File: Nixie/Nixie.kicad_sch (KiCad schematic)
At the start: 43 parts

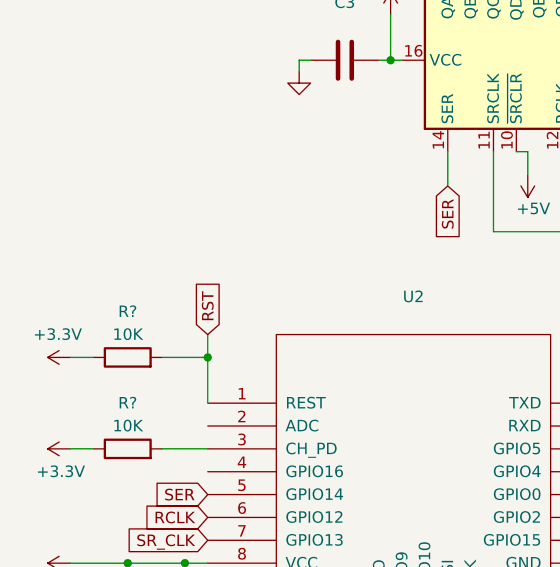
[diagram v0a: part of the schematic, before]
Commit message: Reset Knopf hinzugefügt
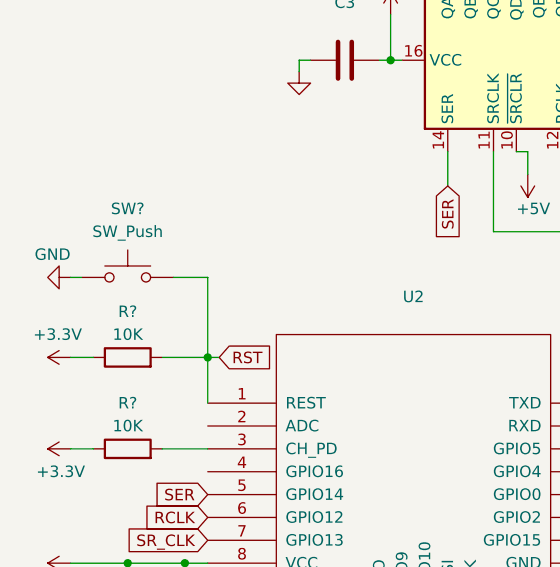
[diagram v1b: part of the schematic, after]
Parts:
- added SW?: SW_Push, symbol Switch:SW_Push
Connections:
- net GND: now also SW?.1
- net RST: now also SW?.2
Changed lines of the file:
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@@
     (stroke (width 0) (type default) (color 0 0 0 0))
   )
-  (wire (pts (xy 33.02 130.81) (xy 33.02 133.35))
+  (wire (pts (xy 34.29 133.35) (xy 33.02 133.35))
     (stroke (width 0) (type default) (color 0 0 0 0))
   )
@@
     (stroke (width 0) (type default) (color 0 0 0 0))
   )
+  (wire (pts (xy 33.02 124.46) (xy 29.21 124.46))
+    (stroke (width 0) (type default) (color 0 0 0 0))
+  )
   (wire (pts (xy 101.6 121.92) (xy 163.83 121.92))
     (stroke (width 0) (type default) (color 0 0 0 0))
@@
     (stroke (width 0) (type default) (color 0 0 0 0))
   )
+  (wire (pts (xy 33.02 133.35) (xy 33.02 124.46))
+    (stroke (width 0) (type default) (color 0 0 0 0))
+  )
   (wire (pts (xy 109.22 67.31) (xy 109.22 69.85))
     (stroke (width 0) (type default) (color 0 0 0 0))
@@
   )
   (wire (pts (xy 165.1 67.31) (xy 166.37 67.31))
+    (stroke (width 0) (type default) (color 0 0 0 0))
+  )
+  (wire (pts (xy 17.78 124.46) (xy 19.05 124.46))
     (stroke (width 0) (type default) (color 0 0 0 0))
   )
@@
     )
   )
-  (global_label "RST" (shape input) (at 33.02 130.81 90) (fields_autoplaced)
+  (global_label "RST" (shape input) (at 34.29 133.35 0) (fields_autoplaced)
     (effects (font (size 1.27 1.27)) (justify left))
-    (property "Referenzen zwischen Schaltplänen" "${INTERSHEET_REFS}" (id 0) (at 171.45 97.79 0)
+    (property "Referenzen zwischen Schaltplänen" "${INTERSHEET_REFS}" (id 0) (at 67.31 271.78 0)
       (effects (font (size 1.27 1.27)) hide)
     )
@@
     (pin "5")
   )
+  (symbol (lib_id "power:GND") (at 17.78 124.46 270) (unit 1)
+    (in_bom yes) (on_board yes)
+    (property "Reference" "#PWR?" (id 0) (at 11.43 124.46 0)
+      (effects (font (size 1.27 1.27)) hide)
+    )
+    (property "Value" "GND" (id 1) (at 17.78 121.92 90)
+      (effects (font (size 1.27 1.27)) (justify right))
+    )
+    (property "Footprint" "" (id 2) (at 17.78 124.46 0)
+      (effects (font (size 1.27 1.27)) hide)
+    )
+    (property "Datasheet" "" (id 3) (at 17.78 124.46 0)
+      (effects (font (size 1.27 1.27)) hide)
+    )
+    (pin "1")
+  )
   (symbol (lib_id "Connector:Conn_01x01_Male") (at 243.84 69.85 0) (unit 1)
     (in_bom yes) (on_board yes)
@@
     (pin "2")
   )
+  (symbol (lib_id "Switch:SW_Push") (at 24.13 124.46 0) (unit 1)
+    (in_bom yes) (on_board yes) (fields_autoplaced)
+    (property "Reference" "SW?" (id 0) (at 24.13 116.84 0))
+    (property "Value" "SW_Push" (id 1) (at 24.13 119.38 0))
+    (property "Footprint" "" (id 2) (at 24.13 119.38 0)
+      (effects (font (size 1.27 1.27)) hide)
+    )
+    (property "Datasheet" "~" (id 3) (at 24.13 119.38 0)
+      (effects (font (size 1.27 1.27)) hide)
+    )
+    (pin "1")
+    (pin "2")
+  )
   (symbol (lib_id "Transistor_BJT:BC547") (at 147.32 142.24 0) (unit 1)
     (in_bom yes) (on_board yes) (fields_autoplaced)
@@
       (reference "#PWR?") (unit 1) (value "+3.3V") (footprint "")
     )
+    (path "/25ee37bc-75c4-4196-949f-55165a570115"
+      (reference "#PWR?") (unit 1) (value "GND") (footprint "")
+    )
     (path "/3d3820fb-53be-4c23-a418-f1d3140026b3"
       (reference "#PWR?") (unit 1) (value "+5V") (footprint "")
@@
       (reference "R?") (unit 1) (value "10K") (footprint "")
     )
+    (path "/626ebd10-8e14-4655-a353-0bf04900a6e8"
+      (reference "SW?") (unit 1) (value "SW_Push") (footprint "")
+    )
     (path "/00000000-0000-0000-0000-0000604e13ef"

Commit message: Platine begonnen
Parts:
- removed C?: 470pF, symbol Device:C
- removed J? (x4): Conn_01x01_Male, symbol Connector:Conn_01x01_Male
- removed Q? (x2): BC547, Package_TO_SOT_THT:TO-92_Inline, symbol Transistor_BJT:BC547
- removed R? (x3): 10K, symbol Device:R
- removed SW?: SW_Push, symbol Switch:SW_Push
- removed U2: (no value), symbol Nixie-rescue:ESP-12F-ESP8266
- added C8: 470pF, Capacitor_SMD:C_1206_3216Metric_Pad1.33x1.80mm_HandSolder, symbol Device:C
- added Q1, Q2: BC847, Package_TO_SOT_SMD:SOT-23, symbol Transistor_BJT:BC847
- added R1, R2, R5: 10K, Resistor_SMD:R_1206_3216Metric_Pad1.30x1.75mm_HandSolder, symbol Device:R
- added SW1: SW_Push, Button_Switch_SMD:SW_Push_1P1T_NO_CK_KSC7xxJ, symbol Switch:SW_Push
- added U2: ESP-12E, RF_Module:ESP-12E, symbol RF_Module:ESP-12E
- added U9: NCH8200HV, nch_psu:NCH8200HV, symbol NCH8200HV:NCH8200HV
- C1, C2, C3, C4, C5, C6, C7: value (none) -> 0.1uF; footprint (none) -> Capacitor_SMD:C_1210_3225Metric_Pad1.33x2.70mm_HandSolder
- C10, C9: renamed from C?; value (none) -> 330uF; footprint (none) -> Capacitor_SMD:CP_Elec_5x3
- D1: renamed from D?; value (none) -> 1N5819; footprint (none) -> Diode_THT:D_DO-41_SOD81_P10.16mm_Horizontal
- H1, H2, H3, H4: value (none) -> MountingHole_Pad; footprint (none) -> MountingHole:MountingHole_3.2mm_M3_Pad
- J1: renamed from J?; footprint (none) -> Connector_PinHeader_2.54mm:PinHeader_1x05_P2.54mm_Vertical
- J2: renamed from J?; value (none) -> USB_B_Micro; footprint (none) -> Connector_USB:USB_Micro-B_Molex-105017-0001
- L1: renamed from L?; value (none) -> 330uH; footprint (none) -> Inductor_SMD:L_1812_4532Metric_Pad1.30x3.40mm_HandSolder
- N1, N2, N3, N4: value (none) -> IN-16; footprint (none) -> in-16:russian-nixies-IN-16
- R10, R3, R4, R7: value (none) -> 10k; footprint (none) -> Resistor_SMD:R_1206_3216Metric_Pad1.30x1.75mm_HandSolder
- U1, U4, U5, U7: value (none) -> K155ID1; footprint (none) -> Package_DIP:DIP-16_W7.62mm_Socket
- U3: value (none) -> 74HC595; footprint (none) -> Package_SO:SOIC-16_4.55x10.3mm_P1.27mm
- U6: value (none) -> 74HC595; footprint (none) -> Package_SO:SOIC-16_3.9x9.9mm_P1.27mm
- U8: renamed from U?; value (none) -> LM2575-3.3BT; footprint (none) -> Package_TO_SOT_THT:TO-220-5_Vertical
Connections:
- net +3.3V: now also C8.1, R1.1, R2.1, U2.8 (VCC)
- net +5V: now also U9.1 (VIN)
- net 170V: now also U9.4 (170V)
- net DTR: now also Q1.1 (B), Q2.2 (E)
- net GND: now also C8.2, R5.1, SW1.1, U2.15 (GND), U9.2 (GND), U9.3 (GND)
- net GPIO0: now also Q2.3 (C), U2.18 (GPIO0)
- net RCLK: now also U2.6 (GPIO12)
- net RST: now also Q1.3 (C), R1.2, SW1.2, U2.1 (~{RST})
- net RTS: now also Q1.2 (E), Q2.1 (B)
- net SER: now also U2.5 (GPIO14)
- net SR_CLK: now also U2.7 (GPIO13)
- net RX: now reaches J1.1 (Pin_1)
- net RX: now also U2.21 (GPIO3/RXD)
- net TX: now reaches J1.2 (Pin_2)
- net TX: now also U2.22 (GPIO1/TXD)
- new net: R5.2, U2.16 (GPIO15)
- new net: R2.2, U2.3 (EN)
- no-connect marks 9 -> 20

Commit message: Platinenlayout begonnen
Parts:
- removed U9: NCH8200HV, nch_psu:NCH8200HV, symbol NCH8200HV:NCH8200HV
- added U9: NCH8200HV, nch_psu:NCH8200HV, symbol psu:NCH8200HV
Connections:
- net +5V: now also U9.1 (Vin)
- net 170V: now also U9.3 (Vout)
- net DTR: now also J1.4 (Pin_4); no longer J1.3 (Pin_3)
- net GND: now also U1.12 (GND), U4.12 (GND), U5.12 (GND), U7.12 (GND), U9.2 (GND), U9.4 (GND); no longer U1.~ (GND), U4.~ (GND), U5.~ (GND), U7.~ (GND)
- net RTS: now also J1.3 (Pin_3); no longer J1.4 (Pin_4)
- net RX: now also J1.2 (Pin_2); no longer J1.1 (Pin_1)
- net TX: now also J1.1 (Pin_1); no longer J1.2 (Pin_2)

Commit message: Added missing footprints to project
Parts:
- U9: footprint nch_psu:NCH8200HV -> psu:NCH8200HV
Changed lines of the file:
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@@
     (property "Reference" "U9" (id 0) (at 236.22 63.5 0))
     (property "Value" "NCH8200HV" (id 1) (at 236.22 66.04 0))
-    (property "Footprint" "nch_psu:NCH8200HV" (id 2) (at 246.38 77.47 0)
+    (property "Footprint" "psu:NCH8200HV" (id 2) (at 246.38 77.47 0)
       (effects (font (size 1.27 1.27)) hide)
     )
@@
     )
     (path "/119f5af4-6f40-4dad-a568-cf0ab1bbe09b"
-      (reference "U9") (unit 1) (value "NCH8200HV") (footprint "nch_psu:NCH8200HV")
-    )
-  )
+      (reference "U9") (unit 1) (value "NCH8200HV") (footprint "psu:NCH8200HV")
+    )
+  )

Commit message: Designed 2-layer PCB
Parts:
- U3: footprint Package_SO:SOIC-16_4.55x10.3mm_P1.27mm -> Package_SO:SOIC-16_3.9x9.9mm_P1.27mm
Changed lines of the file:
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@@
       (effects (font (size 1.27 1.27)) (justify right))
     )
-    (property "Footprint" "Package_SO:SOIC-16_4.55x10.3mm_P1.27mm" (id 2) (at 69.85 100.33 0)
+    (property "Footprint" "Package_SO:SOIC-16_3.9x9.9mm_P1.27mm" (id 2) (at 69.85 100.33 0)
       (effects (font (size 1.27 1.27)) hide)
     )
@@
     )
     (path "/00000000-0000-0000-0000-00006050fca2"
-      (reference "U3") (unit 1) (value "74HC595") (footprint "Package_SO:SOIC-16_4.55x10.3mm_P1.27mm")
+      (reference "U3") (unit 1) (value "74HC595") (footprint "Package_SO:SOIC-16_3.9x9.9mm_P1.27mm")
     )
     (path "/7caced0f-08f6-470b-b067-23373c63af8d"

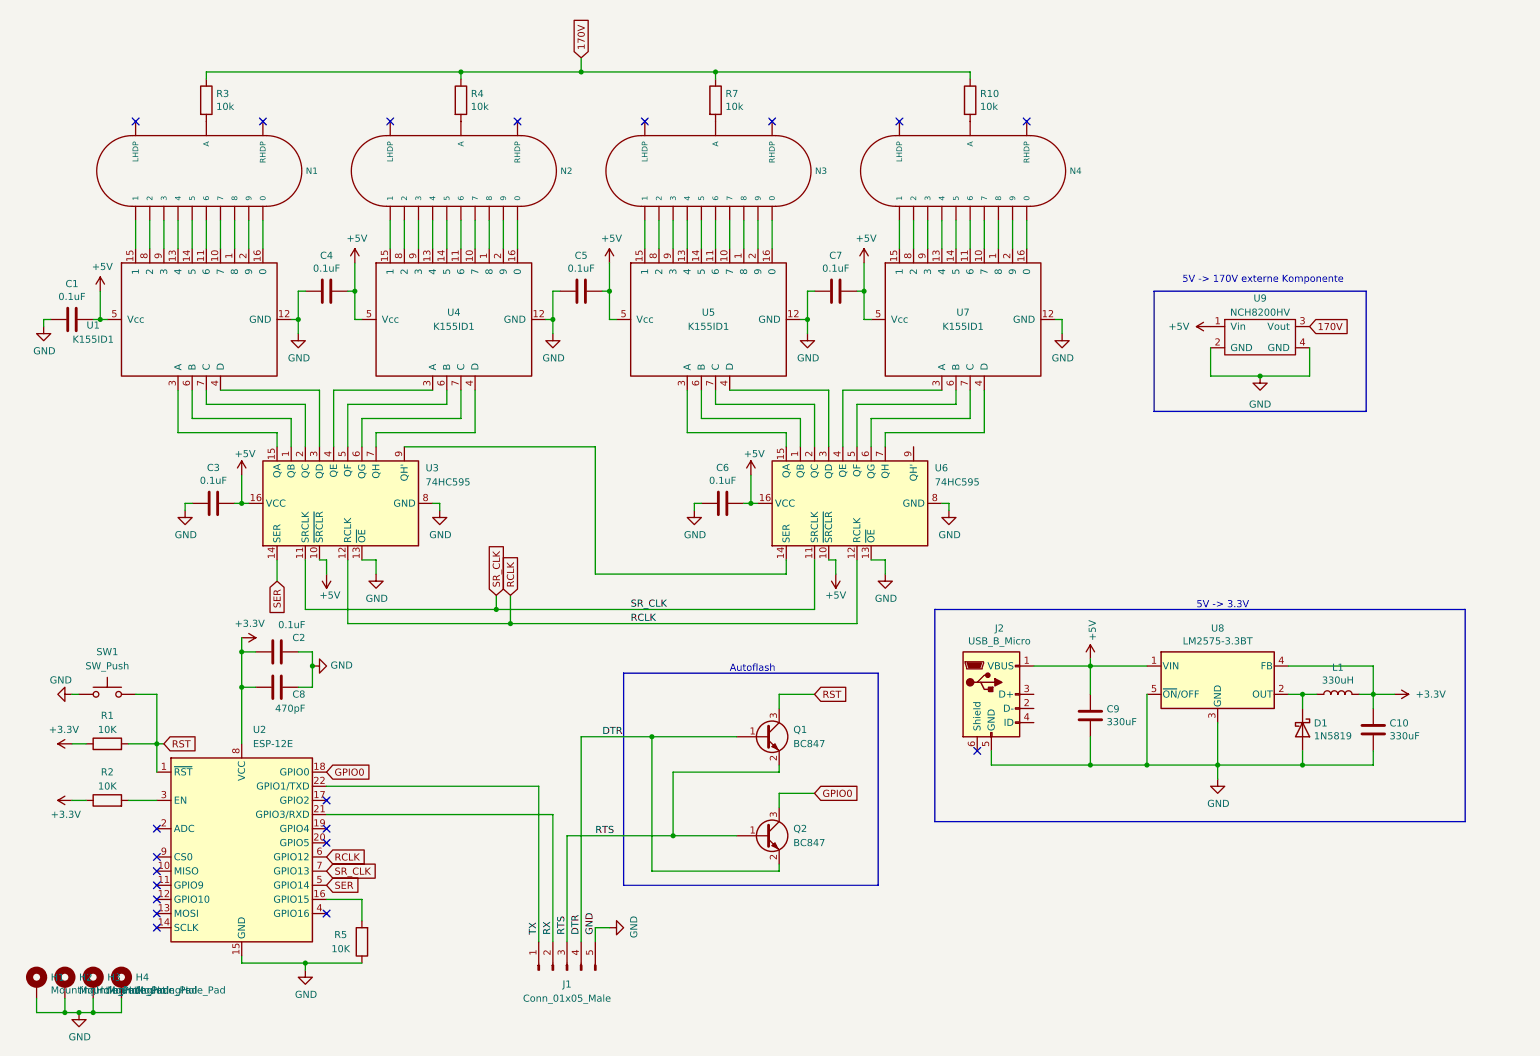
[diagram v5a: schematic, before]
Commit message: Platine neu gezeichnet mit gmit genauen Maßen
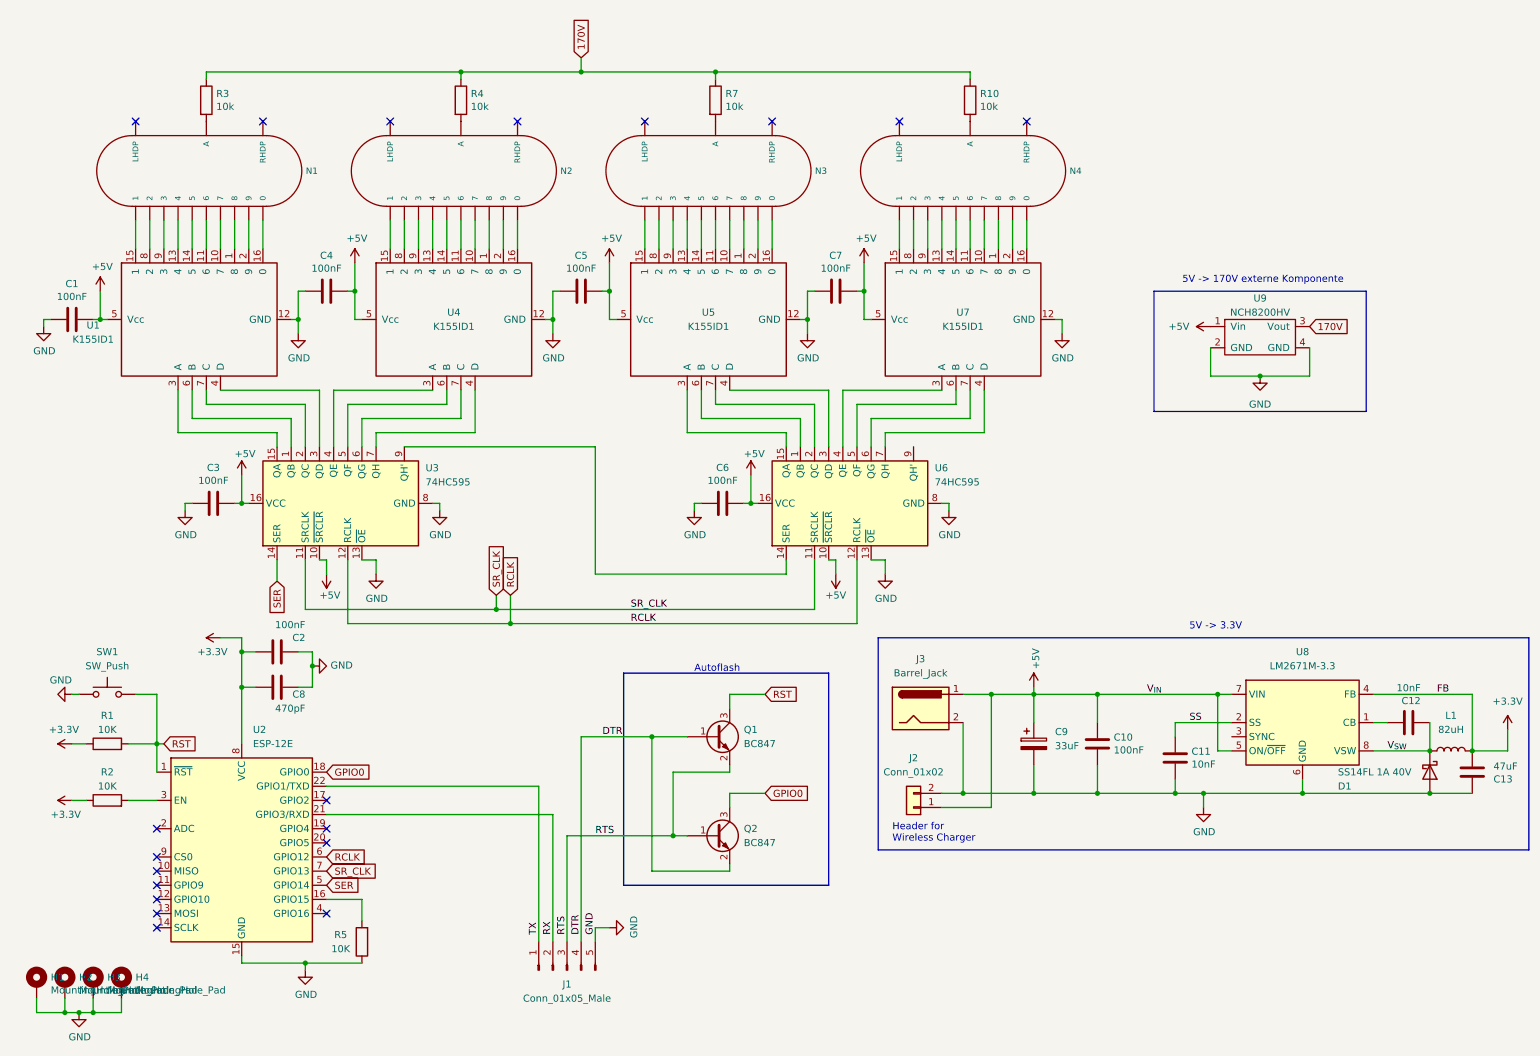
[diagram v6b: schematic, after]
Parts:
- removed C9: 330uF, Capacitor_SMD:CP_Elec_5x3, symbol Device:C
- removed D1: 1N5819, Diode_THT:D_DO-41_SOD81_P10.16mm_Horizontal, symbol Diode:1N5819
- removed J2: USB_B_Micro, Connector_USB:USB_Micro-B_Molex-105017-0001, symbol Connector:USB_B_Micro
- removed U8: LM2575-3.3BT, Package_TO_SOT_THT:TO-220-5_Vertical, symbol Regulator_Switching:LM2575-3.3BT
- added C11, C12: 10nF, Capacitor_SMD:C_0603_1608Metric, symbol Device:C
- added C13: 47uF, Capacitor_SMD:C_0603_1608Metric, symbol Device:C
- added C9: 33uF, Capacitor_SMD:CP_Elec_4x4.5, symbol Device:C_Polarized
- added D1: SS14FL 1A 40V, diode:D_SMA, symbol Device:D_Schottky
- added J2: Conn_01x02, Connector_JST:JST_EH_B2B-EH-A_1x02_P2.50mm_Vertical, symbol Connector_Generic:Conn_01x02
- added J3: Barrel_Jack, Connector_BarrelJack:BarrelJack_Horizontal, symbol Connector:Barrel_Jack
- added U8: LM2671M-3.3, Package_SO:SOIC-8_3.9x4.9mm_P1.27mm, symbol Regulator_Switching:LM2672M-3.3
- C1, C2, C3, C4, C5, C6, C7: value 0.1uF -> 100nF; footprint Capacitor_SMD:C_1210_3225Metric_Pad1.33x2.70mm_HandSolder -> Capacitor_SMD:C_0603_1608Metric_Pad1.08x0.95mm_HandSolder
- C10: value 330uF -> 100nF; footprint Capacitor_SMD:CP_Elec_5x3 -> Capacitor_SMD:C_0603_1608Metric
- C8: footprint Capacitor_SMD:C_1206_3216Metric_Pad1.33x1.80mm_HandSolder -> Capacitor_SMD:C_0603_1608Metric_Pad1.08x0.95mm_HandSolder
- L1: value 330uH -> 82uH; footprint Inductor_SMD:L_1812_4532Metric_Pad1.30x3.40mm_HandSolder -> Inductor_SMD:L_1210_3225Metric
- R1, R10, R2, R3, R4, R5, R7: footprint Resistor_SMD:R_1206_3216Metric_Pad1.30x1.75mm_HandSolder -> Resistor_SMD:R_0603_1608Metric_Pad0.98x0.95mm_HandSolder
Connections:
- net +3.3V: now also C13.1, U8.4 (FB); no longer C10.1
- net +5V: now also C10.1, C9.1, J2.1 (Pin_1), J3.1, U8.5 (ON/~{OFF}), U8.7 (VIN)
- net GND: now also C11.2, C13.2, C9.2, D1.2 (A), J2.2 (Pin_2), J3.2, U8.6 (GND)
- net V_{SW}: now reaches L1.1
- net V_{SW}: now also C12.2, D1.1 (K), U8.8 (VSW)
- new net: C12.1, U8.1 (CB)
- new net SS: C11.1, U8.2 (SS)
- no-connect marks 20 -> 19
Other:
- note added: "Header for Wireless Charger"
- moved on the sheet: Q1, Q2
